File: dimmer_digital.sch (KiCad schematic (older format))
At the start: 25 parts, among them J1 AVR-ISP-6, J2 Conn_01x02, J3 Conn_01x02, J4 Screw_Terminal_01x02, J5 Screw_Terminal_01x02, Q1 TIC226, SW1 SW_DPDT_x2, SW2 SW_Push, U1 ATtiny13A-PU, U2 MOC3021M, U3 4N25

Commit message: Footprints
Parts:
- C1, C2, C3: footprint (none) -> Capacitor_THT:CP_Radial_D5.0mm_P2.50mm
- D1, D2: footprint (none) -> LED_THT:LED_D3.0mm
- J1: footprint (none) -> Connector_PinHeader_2.54mm:PinHeader_2x03_P2.54mm_Vertical
- J2, J3: footprint (none) -> Connector_PinHeader_2.54mm:PinHeader_1x02_P2.54mm_Vertical
- J4, J5: footprint (none) -> TerminalBlock:TerminalBlock_bornier-2_P5.08mm
- R1, R2, R4, R5, R6, R7: footprint (none) -> Resistor_THT:R_Axial_DIN0207_L6.3mm_D2.5mm_P7.62mm_Horizontal
- R3: value R -> 47kΩ; footprint (none) -> Resistor_THT:R_Axial_DIN0207_L6.3mm_D2.5mm_P7.62mm_Horizontal
- RV1, SW1: footprint (none) -> Connector_PinHeader_2.54mm:PinHeader_1x03_P2.54mm_Vertical
- SW2: footprint (none) -> Button_Switch_THT:SW_PUSH_6mm
- U1: footprint Package_DIP:DIP-8_W7.62mm -> Package_DIP:DIP-8_W7.62mm_Socket
- U2: footprint (none) -> Package_DIP:DIP-6_W7.62mm_Socket
- U3: footprint Package_DIP:DIP-6_W7.62mm -> Package_DIP:DIP-6_W7.62mm_Socket
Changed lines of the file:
@@
 P 6200 2330
 F 0 "R3" V 5993 2330 50  0000 C CNN
-F 1 "R" V 6084 2330 50  0000 C CNN
-F 2 "" V 6130 2330 50  0001 C CNN
+F 1 "47kΩ" V 6084 2330 50  0000 C CNN
+F 2 "Resistor_THT:R_Axial_DIN0207_L6.3mm_D2.5mm_P7.62mm_Horizontal" V 6130 2330 50  0001 C CNN
 F 3 "~" H 6200 2330 50  0001 C CNN
 	1    6200 2330
@@
 F 0 "U1" H 1921 1646 50  0000 R CNN
 F 1 "ATtiny13A-PU" H 1921 1555 50  0000 R CNN
-F 2 "Package_DIP:DIP-8_W7.62mm" H 2450 1600 50  0001 C CIN
+F 2 "Package_DIP:DIP-8_W7.62mm_Socket" H 2450 1600 50  0001 C CIN
 F 3 "http://ww1.microchip.com/downloads/en/DeviceDoc/doc8126.pdf" H 2450 1600 50  0001 C CNN
 	1    2450 1600
@@
 F 0 "R4" V 6163 960 50  0000 C CNN
 F 1 "330Ω" V 6254 960 50  0000 C CNN
-F 2 "" V 6300 960 50  0001 C CNN
+F 2 "Resistor_THT:R_Axial_DIN0207_L6.3mm_D2.5mm_P7.62mm_Horizontal" V 6300 960 50  0001 C CNN
 F 3 "~" H 6370 960 50  0001 C CNN
 	1    6370 960
@@
 F 0 "D2" H 6693 705 50  0000 C CNN
 F 1 "LED" H 6693 796 50  0000 C CNN
-F 2 "" H 6700 960 50  0001 C CNN
+F 2 "LED_THT:LED_D3.0mm" H 6700 960 50  0001 C CNN
 F 3 "~" H 6700 960 50  0001 C CNN
 	1    6700 960
@@
 F 0 "C3" V 6785 1360 50  0000 C CNN
 F 1 "10µF" V 6694 1360 50  0000 C CNN
-F 2 "" H 6568 1210 50  0001 C CNN
+F 2 "Capacitor_THT:CP_Radial_D5.0mm_P2.50mm" H 6568 1210 50  0001 C CNN
 F 3 "~" H 6530 1360 50  0001 C CNN
 	1    6530 1360
@@
 F 0 "SW1" V 2004 3548 50  0000 L CNN
 F 1 "SW_DPDT_x2" V 2095 3548 50  0000 L CNN
-F 2 "" H 2050 3400 50  0001 C CNN
+F 2 "Connector_PinHeader_2.54mm:PinHeader_1x03_P2.54mm_Vertical" H 2050 3400 50  0001 C CNN
 F 3 "~" H 2050 3400 50  0001 C CNN
 	1    2050 3400
@@
 F 0 "C1" H 2518 3796 50  0000 L CNN
 F 1 "10µF" H 2518 3705 50  0000 L CNN
-F 2 "" H 2438 3600 50  0001 C CNN
+F 2 "Capacitor_THT:CP_Radial_D5.0mm_P2.50mm" H 2438 3600 50  0001 C CNN
 F 3 "~" H 2400 3750 50  0001 C CNN
 	1    2400 3750
@@
 F 0 "R1" V 2543 3600 50  0000 C CNN
 F 1 "1kΩ" V 2634 3600 50  0000 C CNN
-F 2 "" V 2680 3600 50  0001 C CNN
+F 2 "Resistor_THT:R_Axial_DIN0207_L6.3mm_D2.5mm_P7.62mm_Horizontal" V 2680 3600 50  0001 C CNN
 F 3 "~" H 2750 3600 50  0001 C CNN
 	1    2750 3600
@@
 F 0 "J2" H 9830 2832 50  0000 L CNN
 F 1 "Conn_01x02" H 9830 2741 50  0000 L CNN
-F 2 "" H 9750 2840 50  0001 C CNN
+F 2 "Connector_PinHeader_2.54mm:PinHeader_1x02_P2.54mm_Vertical" H 9750 2840 50  0001 C CNN
 F 3 "~" H 9750 2840 50  0001 C CNN
 	1    9750 2840
@@
 F 0 "R7" V 7100 2810 50  0000 C CNN
 F 1 "47kΩ" V 7330 2810 50  0000 C CNN
-F 2 "" V 7130 2810 50  0001 C CNN
+F 2 "Resistor_THT:R_Axial_DIN0207_L6.3mm_D2.5mm_P7.62mm_Horizontal" V 7130 2810 50  0001 C CNN
 F 3 "~" H 7200 2810 50  0001 C CNN
 	1    7200 2810
@@
 F 0 "U3" H 6750 3035 50  0000 C CNN
 F 1 "4N25" H 6750 2944 50  0000 C CNN
-F 2 "Package_DIP:DIP-6_W7.62mm" H 6550 2510 50  0001 L CIN
+F 2 "Package_DIP:DIP-6_W7.62mm_Socket" H 6550 2510 50  0001 L CIN
 F 3 "https://www.vishay.com/docs/83725/4n25.pdf" H 6750 2710 50  0001 L CNN
 	1    6750 2710
@@
 F 0 "R6" V 6993 2610 50  0000 C CNN
 F 1 "47kΩ" V 7084 2610 50  0000 C CNN
-F 2 "" V 7130 2610 50  0001 C CNN
+F 2 "Resistor_THT:R_Axial_DIN0207_L6.3mm_D2.5mm_P7.62mm_Horizontal" V 7130 2610 50  0001 C CNN
 F 3 "~" H 7200 2610 50  0001 C CNN
 	1    7200 2610
@@
 F 0 "R5" V 6943 4300 50  0000 C CNN
 F 1 "1kΩ" V 7034 4300 50  0000 C CNN
-F 2 "" V 7080 4300 50  0001 C CNN
+F 2 "Resistor_THT:R_Axial_DIN0207_L6.3mm_D2.5mm_P7.62mm_Horizontal" V 7080 4300 50  0001 C CNN
 F 3 "~" H 7150 4300 50  0001 C CNN
 	1    7150 4300
@@
 F 0 "D1" H 5893 4245 50  0000 C CNN
 F 1 "LED" H 5893 4336 50  0000 C CNN
-F 2 "" H 5900 4500 50  0001 C CNN
+F 2 "LED_THT:LED_D3.0mm" H 5900 4500 50  0001 C CNN
 F 3 "~" H 5900 4500 50  0001 C CNN
 	1    5900 4500
@@
 F 0 "R2" V 5393 4500 50  0000 C CNN
 F 1 "330Ω" V 5484 4500 50  0000 C CNN
-F 2 "" V 5530 4500 50  0001 C CNN
+F 2 "Resistor_THT:R_Axial_DIN0207_L6.3mm_D2.5mm_P7.62mm_Horizontal" V 5530 4500 50  0001 C CNN
 F 3 "~" H 5600 4500 50  0001 C CNN
 	1    5600 4500
@@
 F 0 "U2" H 6400 4925 50  0000 C CNN
 F 1 "MOC3021M" H 6400 4834 50  0000 C CNN
-F 2 "" H 6200 4400 50  0001 L CIN
+F 2 "Package_DIP:DIP-6_W7.62mm_Socket" H 6200 4400 50  0001 L CIN
 F 3 "http://www.fairchildsemi.com/ds/MO/MOC3020M.pdf" H 6400 4600 50  0001 L CNN
 	1    6400 4600
@@
 F 0 "J5" H 9830 1942 50  0000 L CNN
 F 1 "Screw_Terminal_01x02" H 9830 1851 50  0000 L CNN
-F 2 "" H 9750 1950 50  0001 C CNN
+F 2 "TerminalBlock:TerminalBlock_bornier-2_P5.08mm" H 9750 1950 50  0001 C CNN
 F 3 "~" H 9750 1950 50  0001 C CNN
 	1    9750 1950
@@
 F 0 "RV1" H 1531 3646 50  0000 R CNN
 F 1 "R_POT" H 1531 3555 50  0000 R CNN
-F 2 "" H 1600 3600 50  0001 C CNN
+F 2 "Connector_PinHeader_2.54mm:PinHeader_1x03_P2.54mm_Vertical" H 1600 3600 50  0001 C CNN
 F 3 "~" H 1600 3600 50  0001 C CNN
 	1    1600 3600
@@
 F 0 "J4" H 9830 1042 50  0000 L CNN
 F 1 "Screw_Terminal_01x02" H 9830 951 50  0000 L CNN
-F 2 "" H 9750 1050 50  0001 C CNN
+F 2 "TerminalBlock:TerminalBlock_bornier-2_P5.08mm" H 9750 1050 50  0001 C CNN
 F 3 "~" H 9750 1050 50  0001 C CNN
 	1    9750 1050
@@
 F 0 "J1" H 4061 6836 50  0000 R CNN
 F 1 "AVR-ISP-6" H 4061 6745 50  0000 R CNN
-F 2 "" V 4140 6790 50  0001 C CNN
+F 2 "Connector_PinHeader_2.54mm:PinHeader_2x03_P2.54mm_Vertical" V 4140 6790 50  0001 C CNN
 F 3 " ~" H 3115 6190 50  0001 C CNN
 	1    4390 6740
@@
 F 0 "SW2" H 2280 5575 50  0000 C CNN
 F 1 "SW_Push" H 2280 5484 50  0000 C CNN
-F 2 "" H 2280 5490 50  0001 C CNN
+F 2 "Button_Switch_THT:SW_PUSH_6mm" H 2280 5490 50  0001 C CNN
 F 3 "~" H 2280 5490 50  0001 C CNN
 	1    2280 5290
@@
 F 0 "C2" H 2618 5596 50  0000 L CNN
 F 1 "10µF" H 2618 5505 50  0000 L CNN
-F 2 "" H 2538 5400 50  0001 C CNN
+F 2 "Capacitor_THT:CP_Radial_D5.0mm_P2.50mm" H 2538 5400 50  0001 C CNN
 F 3 "~" H 2500 5550 50  0001 C CNN
 	1    2500 5550
@@
 F 0 "J3" H 9830 4082 50  0000 L CNN
 F 1 "Conn_01x02" H 9830 3991 50  0000 L CNN
-F 2 "" H 9750 4090 50  0001 C CNN
+F 2 "Connector_PinHeader_2.54mm:PinHeader_1x02_P2.54mm_Vertical" H 9750 4090 50  0001 C CNN
 F 3 "~" H 9750 4090 50  0001 C CNN
 	1    9750 4090

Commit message: Update page, added headers for attiny13a, started pcb layout
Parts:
- added J2: CONECTOR_LEFT, Connector_PinHeader_2.54mm:PinHeader_1x04_P2.54mm_Vertical, symbol Connector_Generic:Conn_01x04
- J3: renamed from J2; value Conn_01x02 -> CONNECTOR_SPEED
- J4: value Screw_Terminal_01x02 -> TERMINAL_AC
- J5: value Screw_Terminal_01x02 -> TERMINAL_LOAD
- J6: renamed from J3; value Conn_01x02 -> CONECTOR_RIGHT; footprint Connector_PinHeader_2.54mm:PinHeader_1x02_P2.54mm_Vertical -> Connector_PinHeader_2.54mm:PinHeader_1x04_P2.54mm_Vertical; symbol Connector_Generic:Conn_01x02 -> Connector_Generic:Conn_01x04
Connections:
- net +5V: now also J6.1 (Pin_1)
- net CROSSOVER: now also J6.3 (Pin_3)
- net GND: now also J2.4 (Pin_4)
- net PHASE_CONTROL: now also J6.4 (Pin_4)
- net RESET: now also J2.1 (Pin_1)
- net SPEED_POT: now also J2.3 (Pin_3)
- net UNDEFINED1: now also J6.2 (Pin_2); no longer J6.1 (Pin_1)
- net UNDEFINED2: now also J2.2 (Pin_2); no longer J6.2 (Pin_2)
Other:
- moved on the sheet: J3, PS1

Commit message: wiring complete
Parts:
- removed J1: AVR-ISP-6, Connector_PinHeader_2.54mm:PinHeader_2x03_P2.54mm_Vertical, symbol Connector:AVR-ISP-6
- SW1: value SW_DPDT_x2 -> SWITCH_SPEED
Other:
- note removed: "ICSP Header"
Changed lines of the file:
@@
 Text GLabel 9160 1950 0    50   Output ~ 0
 LOAD1
-Wire Wire Line
-	4880 6540 4790 6540
-Wire Wire Line
-	4790 6640 4910 6640
-Wire Wire Line
-	4790 6740 4890 6740
-Wire Wire Line
-	4890 6840 4790 6840
-Text GLabel 4890 6840 2    50   Input ~ 0
-RESET
-Text GLabel 4890 6740 2    50   BiDi ~ 0
-UNDEFINED1
-Text GLabel 4910 6640 2    50   Output ~ 0
-PHASE_CONTROL
-Text GLabel 4880 6540 2    50   Input ~ 0
-CROSSOVER
-$Comp
-L power:+5V #PWR07
-U 1 1 5F7D21C8
-P 4290 6240
-F 0 "#PWR07" H 4290 6090 50  0001 C CNN
-F 1 "+5V" H 4305 6413 50  0000 C CNN
-F 2 "" H 4290 6240 50  0001 C CNN
-F 3 "" H 4290 6240 50  0001 C CNN
-	1    4290 6240
-	1    0    0    -1
-$EndComp
-$Comp
-L power:GND #PWR08
-U 1 1 5F7D1BBE
-P 4290 7140
-F 0 "#PWR08" H 4290 6890 50  0001 C CNN
-F 1 "GND" H 4295 6967 50  0000 C CNN
-F 2 "" H 4290 7140 50  0001 C CNN
-F 3 "" H 4290 7140 50  0001 C CNN
-	1    4290 7140
-	1    0    0    -1
-$EndComp
-Text Notes 3730 7450 0    50   ~ 0
-ICSP Header
 Text Notes 900  7550 0    50   ~ 0
 1. Attiny\n2. 1x 10k R\n3. Pushbutton\n4. Switch\n5. 4N25\n6. MOC3021\n7. 1x 1k R\n8. TIC226\n9. 2x 30k R\n------10. 4x Diode (1N4001)\n11. Fuse\n12. 1x Potentiometer\n13. HLK-PM01\n14. ICSP Header\n15. 2x 330ohm R\n17. 2x LED 3mm\n18. 10uF C
@@
 P 2050 3400
 F 0 "SW1" V 2004 3548 50  0000 L CNN
-F 1 "SW_DPDT_x2" V 2095 3548 50  0000 L CNN
+F 1 "SWITCH_SPEED" V 2095 3548 50  0000 L CNN
 F 2 "Connector_PinHeader_2.54mm:PinHeader_1x03_P2.54mm_Vertical" H 2050 3400 50  0001 C CNN
 F 3 "~" H 2050 3400 50  0001 C CNN
@@
 	1    0    0    -1
 $EndComp
-$Comp
-L Connector:AVR-ISP-6 J1
-U 1 1 5F7CF9AE
-P 4390 6740
-F 0 "J1" H 4061 6836 50  0000 R CNN
-F 1 "AVR-ISP-6" H 4061 6745 50  0000 R CNN
-F 2 "Connector_PinHeader_2.54mm:PinHeader_2x03_P2.54mm_Vertical" V 4140 6790 50  0001 C CNN
-F 3 " ~" H 3115 6190 50  0001 C CNN
-	1    4390 6740
-	1    0    0    -1
-$EndComp

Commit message: Finished Rev0
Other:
- note removed: "1. Attiny\n2. 1x 10k R\n3. Pushbutton\n4. Switch\n5. 4N25\n6. MOC3021\n7. 1x 1k R\n8. TIC226\n9. 2x 30k R\n------10. 4x Diode (1N4001)\n11. Fuse\n12. 1x Potentiometer\n13. HLK-PM01\n14. ICSP Header\n15. 2x 330ohm R\n17. 2x LED 3mm\n18. 10uF C"
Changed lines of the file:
@@
 Text GLabel 9160 1950 0    50   Output ~ 0
 LOAD1
-Text Notes 900  7550 0    50   ~ 0
-1. Attiny\n2. 1x 10k R\n3. Pushbutton\n4. Switch\n5. 4N25\n6. MOC3021\n7. 1x 1k R\n8. TIC226\n9. 2x 30k R\n------10. 4x Diode (1N4001)\n11. Fuse\n12. 1x Potentiometer\n13. HLK-PM01\n14. ICSP Header\n15. 2x 330ohm R\n17. 2x LED 3mm\n18. 10uF C
 Text GLabel 2030 5290 0    50   Input ~ 0
 RESET

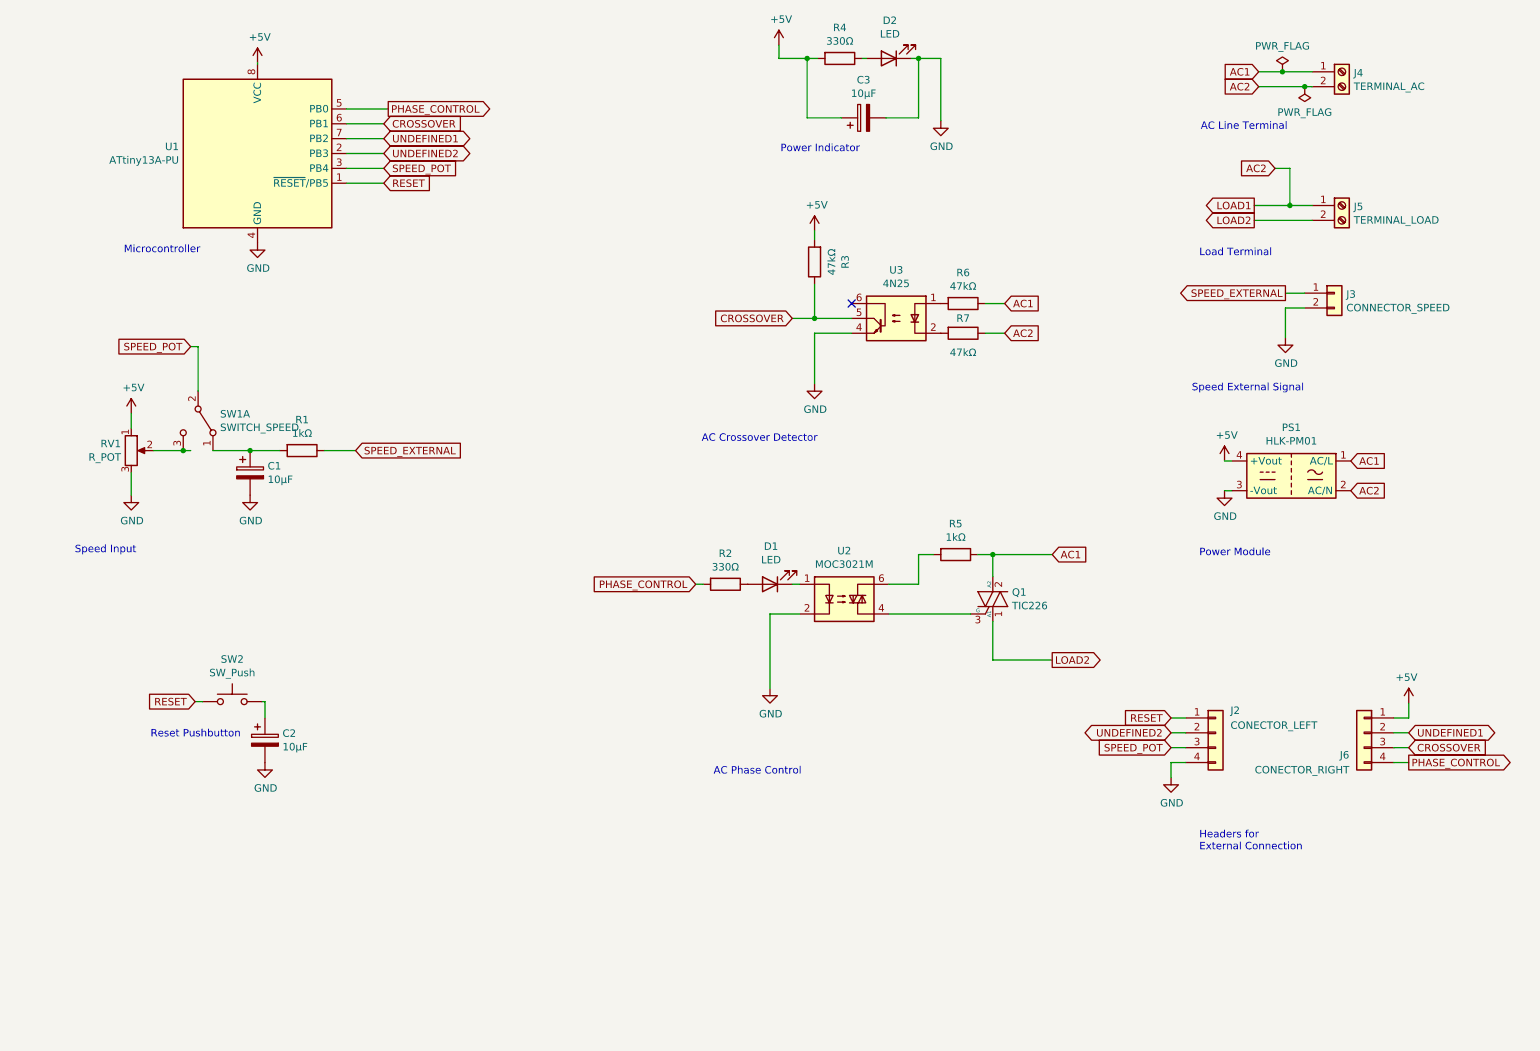
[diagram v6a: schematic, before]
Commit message: Visual update on the schematic
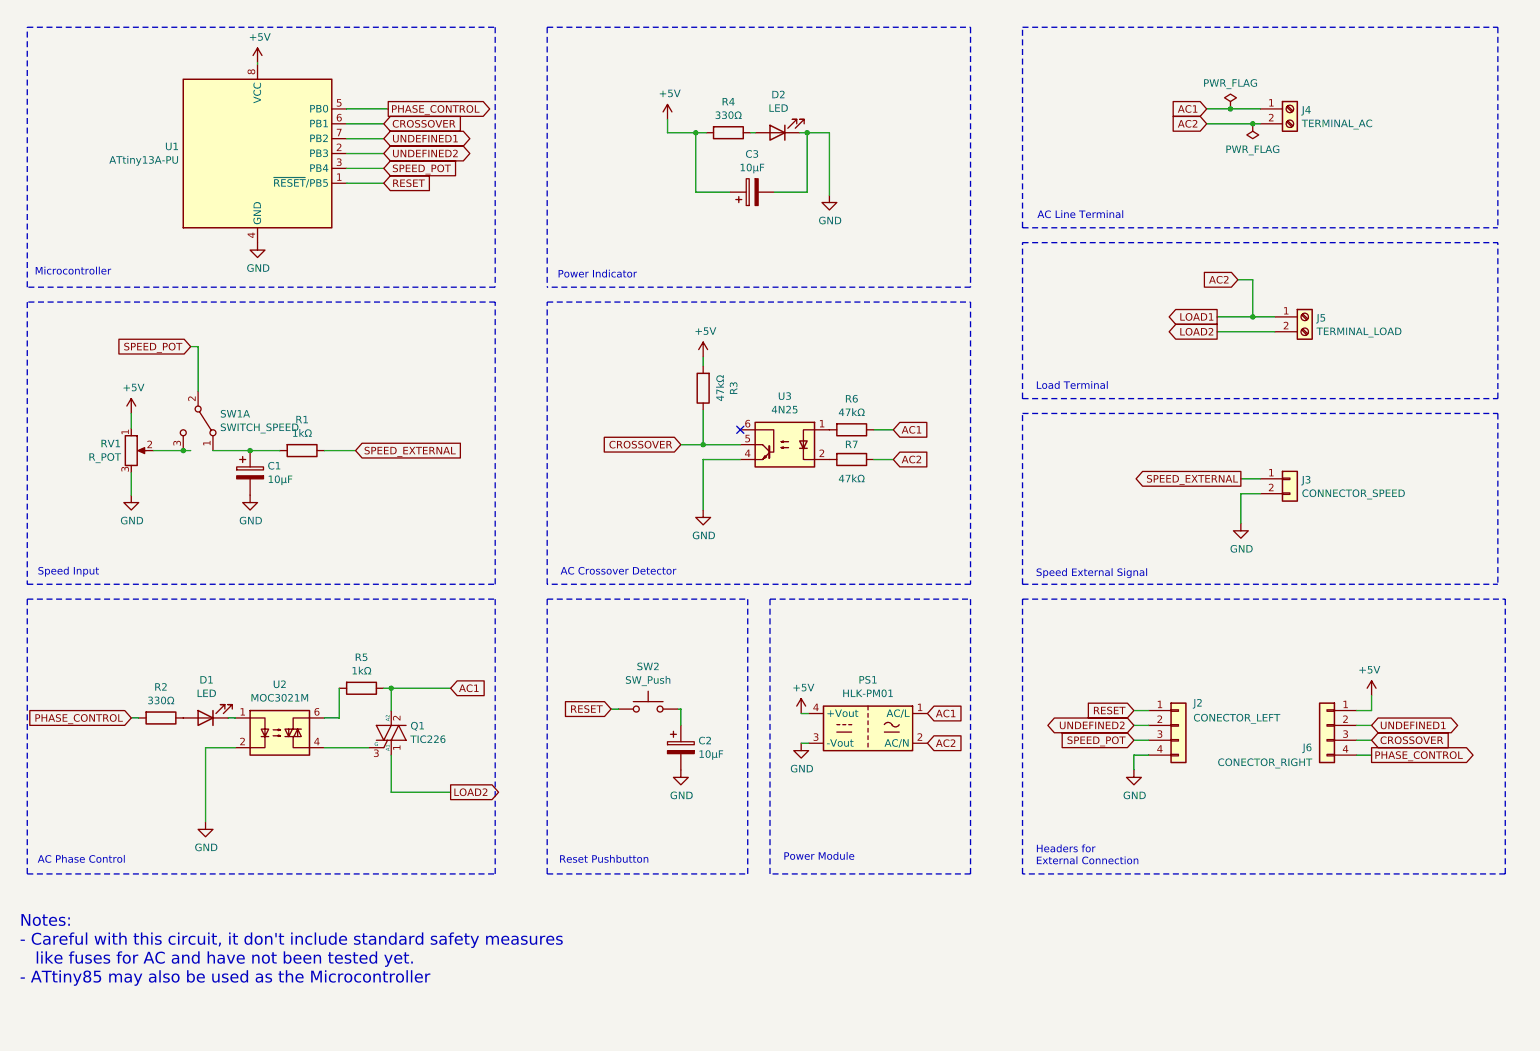
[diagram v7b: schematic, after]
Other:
- note added: "Notes:\n- Careful with this circuit, it don't include standard safety measures \n like fuses for AC and have not been tested yet.\n- ATtiny85 may also be used as the Microcontroller"
- moved on the sheet: C2, C3, D1, D2, J2, J3, J4, J5, J6, PS1, Q1, R2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
